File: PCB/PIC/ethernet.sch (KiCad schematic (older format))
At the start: 49 parts, among them J5 RJ45-TRANSFO, U1 LAN_8740, U2 SI502

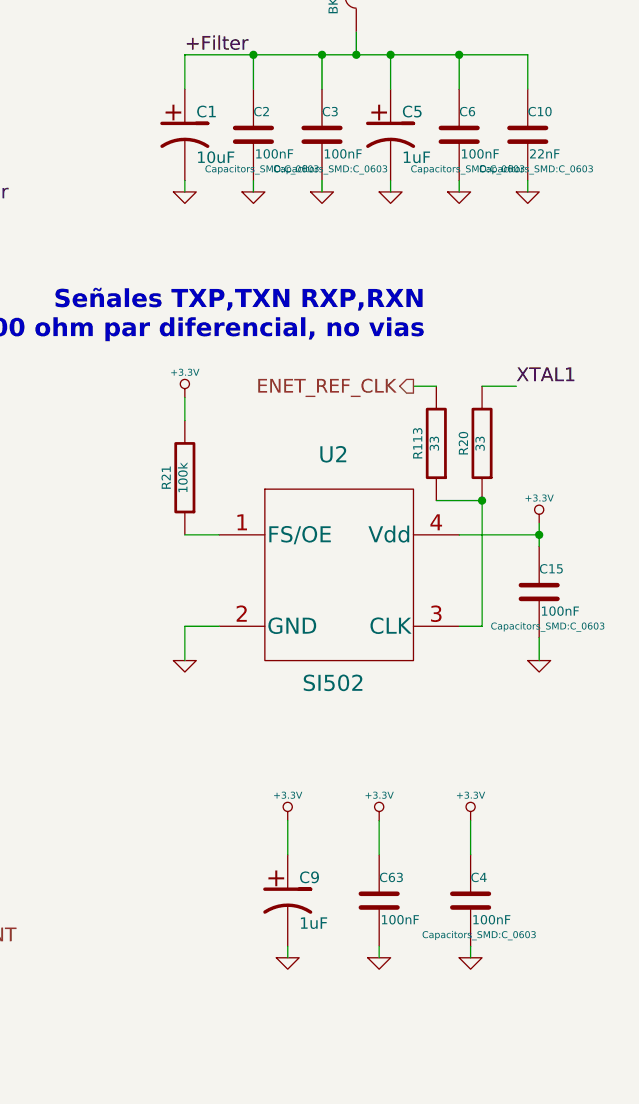
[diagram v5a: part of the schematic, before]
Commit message: rev02 se completa campo num. de frabicante(manf#) CIAA-PIC
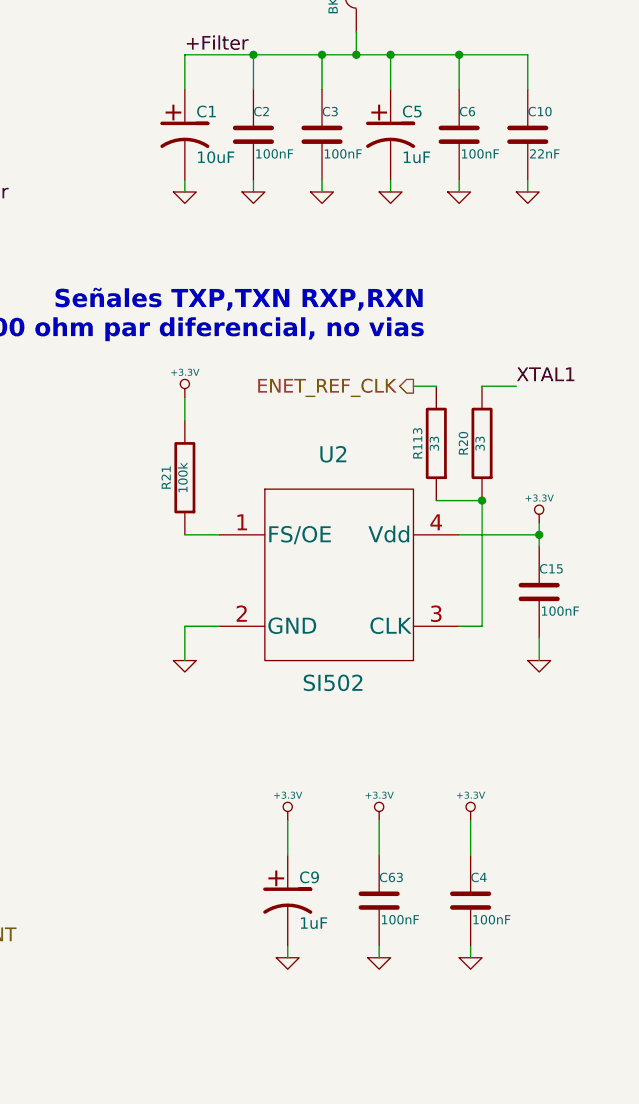
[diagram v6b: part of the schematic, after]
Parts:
- C15, C2, C3, C4, C6, C63: manf# (none) -> C0603C104K5RACTU
- L1: footprint (none) -> footprints:SM0603; manf# (none) -> MH1608-221Y
- R1: manf# (none) -> 311-1.5KGRCT-ND
- R10, R11, R12: manf# (none) -> RC0603JR-0722RL
- R113, R140, R20: manf# (none) -> RC0603JR-0733RL
- R13, R14, R7, R8, R9: manf# (none) -> RC0603JR-070RL
- R139, R2, R31, R81, R91, R95: manf# (none) -> RC0603FR-074K7L
- R15, R16, R92: manf# (none) -> RC0603JR-0710KL
- R17, R18: manf# (none) -> RC0603JR-07270RL
- R19: manf# (none) -> RC0603FR-0712K1L
- R21: manf# (none) -> RC0603JR-07100KL
- R3, R4, R5, R6: #manf RC0603FR-0749R9L -> (none); manf# (none) -> RC0603FR-0749R9L
- U1: manf# (none) -> LAN8740A-EN
- U2: manf# (none) -> 502AAA-ADAG
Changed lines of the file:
@@
 F 0 "C6" H 10350 2350 40  0000 L CNN
 F 1 "100nF" H 10356 2165 40  0000 L CNN
-F 2 "Capacitors_SMD:C_0603" H 10388 2100 30  0000 C CNN
+F 2 "Capacitors_SMD:C_0603" H 10388 2100 30  0001 C CNN
 F 3 "~" H 10350 2250 60  0000 C CNN
+F 4 "C0603C104K5RACTU " H 10350 2250 60  0001 C CNN "manf#"
 	1    10350 2250
 	1    0    0    -1
@@
 F 0 "C2" H 9450 2350 40  0000 L CNN
 F 1 "100nF" H 9456 2165 40  0000 L CNN
-F 2 "Capacitors_SMD:C_0603" H 9488 2100 30  0000 C CNN
+F 2 "Capacitors_SMD:C_0603" H 9488 2100 30  0001 C CNN
 F 3 "~" H 9450 2250 60  0000 C CNN
+F 4 "C0603C104K5RACTU " H 9450 2250 60  0001 C CNN "manf#"
 	1    9450 2250
 	1    0    0    -1
@@
 F 0 "C3" H 9750 2350 40  0000 L CNN
 F 1 "100nF" H 9756 2165 40  0000 L CNN
-F 2 "Capacitors_SMD:C_0603" H 9788 2100 30  0000 C CNN
+F 2 "Capacitors_SMD:C_0603" H 9788 2100 30  0001 C CNN
 F 3 "~" H 9750 2250 60  0000 C CNN
+F 4 "C0603C104K5RACTU " H 9750 2250 60  0001 C CNN "manf#"
 	1    9750 2250
 	1    0    0    -1
@@
 F 2 "Resistors_SMD:R_0603" V 2480 4200 30  0001 C CNN
 F 3 "~" H 2550 4200 30  0000 C CNN
+F 4 "RC0603FR-074K7L" V 2550 4200 60  0001 C CNN "manf#"
 	1    2550 4200
 	1    0    0    -1
@@
 F 2 "Resistors_SMD:R_0603" V 2730 1650 30  0001 C CNN
 F 3 "~" H 2800 1650 30  0000 C CNN
+F 4 "311-1.5KGRCT-ND" V 2800 1650 60  0001 C CNN "manf#"
 	1    2800 1650
 	1    0    0    -1
@@
 F 2 "Resistors_SMD:R_0603" V 6980 2850 30  0001 C CNN
 F 3 "~" H 7050 2850 30  0000 C CNN
-F 4 "RC0603FR-0749R9L" V 7050 2850 60  0001 C CNN "#manf"
+F 4 "RC0603FR-0749R9L" V 7050 2850 60  0001 C CNN "manf#"
 	1    7050 2850
 	1    0    0    -1
@@
 F 2 "Resistors_SMD:R_0603" V 7230 2850 30  0001 C CNN
 F 3 "~" H 7300 2850 30  0000 C CNN
-F 4 "RC0603FR-0749R9L" V 7300 2850 60  0001 C CNN "#manf"
+F 4 "RC0603FR-0749R9L" V 7300 2850 60  0001 C CNN "manf#"
 	1    7300 2850
 	1    0    0    -1
@@
 F 2 "Resistors_SMD:R_0603" V 7580 2850 30  0001 C CNN
 F 3 "~" H 7650 2850 30  0000 C CNN
-F 4 "RC0603FR-0749R9L" V 7650 2850 60  0001 C CNN "#manf"
+F 4 "RC0603FR-0749R9L" V 7650 2850 60  0001 C CNN "manf#"
 	1    7650 2850
 	1    0    0    -1
@@
 F 2 "Resistors_SMD:R_0603" V 7780 2850 30  0001 C CNN
 F 3 "~" H 7850 2850 30  0000 C CNN
-F 4 "RC0603FR-0749R9L" V 7850 2850 60  0001 C CNN "#manf"
+F 4 "RC0603FR-0749R9L" V 7850 2850 60  0001 C CNN "manf#"
 	1    7850 2850
 	1    0    0    -1
@@
 F 0 "C10" H 10650 2350 40  0000 L CNN
 F 1 "22nF" H 10656 2165 40  0000 L CNN
-F 2 "Capacitors_SMD:C_0603" H 10688 2100 30  0000 C CNN
+F 2 "Capacitors_SMD:C_0603" H 10688 2100 30  0001 C CNN
 F 3 "~" H 10650 2250 60  0000 C CNN
 	1    10650 2250
@@
 F 2 "Resistors_SMD:R_0603" V 780 6800 30  0001 C CNN
 F 3 "~" H 850 6800 30  0000 C CNN
+F 4 "RC0603JR-07270RL" V 850 6800 60  0001 C CNN "manf#"
 	1    850  6800
 	-1   0    0    1
@@
 F 2 "Resistors_SMD:R_0603" V 980 6800 30  0001 C CNN
 F 3 "~" H 1050 6800 30  0000 C CNN
+F 4 "RC0603JR-07270RL" V 1050 6800 60  0001 C CNN "manf#"
 	1    1050 6800
 	-1   0    0    1
@@
 F 2 "Resistors_SMD:R_0603" V 7230 5650 30  0001 C CNN
 F 3 "~" H 7300 5650 30  0000 C CNN
+F 4 "RC0603FR-0712K1L " V 7300 5650 60  0001 C CNN "manf#"
 	1    7300 5650
 	1    0    0    -1
@@
 F 0 "C15" H 10700 4350 40  0000 L CNN
 F 1 "100nF" H 10706 4165 40  0000 L CNN
-F 2 "Capacitors_SMD:C_0603" H 10738 4100 30  0000 C CNN
+F 2 "Capacitors_SMD:C_0603" H 10738 4100 30  0001 C CNN
 F 3 "~" H 10700 4250 60  0000 C CNN
+F 4 "C0603C104K5RACTU" H 10700 4250 60  0001 C CNN "manf#"
 	1    10700 4250
 	1    0    0    -1
@@
 F 2 "Resistors_SMD:R_0603" V 1780 2900 30  0001 C CNN
 F 3 "~" H 1850 2900 30  0000 C CNN
+F 4 "RC0603JR-070RL" V 1850 2900 60  0001 C CNN "manf#"
 	1    1850 2900
 	0    -1   -1   0
@@
 F 2 "Resistors_SMD:R_0603" V 1780 3000 30  0001 C CNN
 F 3 "~" H 1850 3000 30  0000 C CNN
+F 4 "RC0603JR-070RL" V 1850 3000 60  0001 C CNN "manf#"
 	1    1850 3000
 	0    -1   -1   0
@@
 F 2 "Resistors_SMD:R_0603" V 1780 2800 30  0001 C CNN
 F 3 "~" H 1850 2800 30  0000 C CNN
+F 4 "RC0603JR-070RL" V 1850 2800 60  0001 C CNN "manf#"
 	1    1850 2800
 	0    -1   -1   0
@@
 F 2 "Resistors_SMD:R_0603" V 1780 2700 30  0001 C CNN
 F 3 "~" H 1850 2700 30  0000 C CNN
+F 4 "RC0603JR-0722RL" V 1850 2700 60  0001 C CNN "manf#"
 	1    1850 2700
 	0    -1   -1   0
@@
 F 2 "Resistors_SMD:R_0603" V 1780 2600 30  0001 C CNN
 F 3 "~" H 1850 2600 30  0000 C CNN
+F 4 "RC0603JR-0722RL" V 1850 2600 60  0001 C CNN "manf#"
 	1    1850 2600
 	0    -1   -1   0
@@
 F 2 "Resistors_SMD:R_0603" V 1930 4550 30  0001 C CNN
 F 3 "~" H 2000 4550 30  0000 C CNN
+F 4 "RC0603JR-0722RL" V 2000 4550 60  0001 C CNN "manf#"
 	1    2000 4550
 	0    -1   -1   0
@@
 F 2 "Resistors_SMD:R_0603" V 1780 2200 30  0001 C CNN
 F 3 "~" H 1850 2200 30  0000 C CNN
+F 4 " RC0603JR-070RL" V 1850 2200 60  0001 C CNN "manf#"
 	1    1850 2200
 	0    -1   -1   0
@@
 F 2 "Resistors_SMD:R_0603" V 1780 2300 30  0001 C CNN
 F 3 "~" H 1850 2300 30  0000 C CNN
+F 4 "RC0603JR-070RL" V 1850 2300 60  0001 C CNN "manf#"
 	1    1850 2300
 	0    -1   -1   0
@@
 F 0 "C4" H 10400 5700 40  0000 L CNN
 F 1 "100nF" H 10406 5515 40  0000 L CNN
-F 2 "Capacitors_SMD:C_0603" H 10438 5450 30  0000 C CNN
+F 2 "Capacitors_SMD:C_0603" H 10438 5450 30  0001 C CNN
 F 3 "~" H 10400 5600 60  0000 C CNN
+F 4 "C0603C104K5RACTU" H 10400 5600 60  0001 C CNN "manf#"
 	1    10400 5600
 	1    0    0    -1
@@
 F 2 "footprints:4SMD" H 9850 3650 60  0001 C CNN
 F 3 "http://www.digikey.com/product-detail/en/silicon-labs/502AAA-ADAG/502AAA-ADAG-ND/4173092" H 8750 7500 60  0001 C CNN
+F 4 "502AAA-ADAG" H 9800 4200 60  0001 C CNN "manf#"
 	1    9800 4200
 	1    0    0    -1
@@
 F 2 "Resistors_SMD:R_0603" V 10380 3600 30  0001 C CNN
 F 3 "~" H 10450 3600 30  0000 C CNN
+F 4 "RC0603JR-0733RL" V 10450 3600 60  0001 C CNN "manf#"
 	1    10450 3600
 	-1   0    0    1
@@
 F 2 "Resistors_SMD:R_0603" V 1780 2500 30  0001 C CNN
 F 3 "~" H 1850 2500 30  0000 C CNN
+F 4 " RC0603JR-0710KL" V 1850 2500 60  0001 C CNN "manf#"
 	1    1850 2500
 	0    -1   -1   0
@@
 F 2 "Resistors_SMD:R_0603" V 7830 5400 30  0001 C CNN
 F 3 "~" H 7900 5400 30  0000 C CNN
+F 4 " RC0603JR-0710KL" V 7900 5400 60  0001 C CNN "manf#"
 	1    7900 5400
 	1    0    0    -1
@@
 F 2 "Resistors_SMD:R_0603" V 9080 3750 30  0001 C CNN
 F 3 "~" H 9150 3750 30  0000 C CNN
+F 4 "RC0603JR-07100KL" V 9150 3750 60  0001 C CNN "manf#"
 	1    9150 3750
 	-1   0    0    1
@@
 F 2 "Resistors_SMD:R_0603" V 2330 1650 30  0001 C CNN
 F 3 "~" H 2400 1650 30  0000 C CNN
+F 4 "RC0603FR-074K7L " V 2400 1650 60  0001 C CNN "manf#"
 	1    2400 1650
 	1    0    0    -1
@@
 F 2 "Capacitors_SMD:C_0603" H 10038 5450 30  0001 C CNN
 F 3 "~" H 10000 5600 60  0000 C CNN
+F 4 "C0603C104K5RACTU" H 10000 5600 60  0001 C CNN "manf#"
 	1    10000 5600
 	1    0    0    -1
@@
 F 2 "Resistors_SMD:R_0603" V 2130 1650 30  0001 C CNN
 F 3 "~" H 2200 1650 30  0000 C CNN
+F 4 "RC0603FR-074K7L " V 2200 1650 60  0001 C CNN "manf#"
 	1    2200 1650
 	1    0    0    -1
@@
 F 2 "Resistors_SMD:R_0603" V 1780 3300 30  0001 C CNN
 F 3 "~" H 1850 3300 30  0000 C CNN
+F 4 "RC0603FR-074K7L " V 1850 3300 60  0001 C CNN "manf#"
 	1    1850 3300
 	0    -1   -1   0
@@
 F 2 "Resistors_SMD:R_0603" V 1780 3200 30  0001 C CNN
 F 3 "~" H 1850 3200 30  0000 C CNN
+F 4 "RC0603FR-074K7L " V 1850 3200 60  0001 C CNN "manf#"
 	1    1850 3200
 	0    -1   -1   0
@@
 F 2 "Resistors_SMD:R_0603" V 1780 2400 30  0001 C CNN
 F 3 "~" H 1850 2400 30  0000 C CNN
+F 4 "RC0603FR-074K7L " V 1850 2400 60  0001 C CNN "manf#"
 	1    1850 2400
 	0    -1   -1   0
@@
 F 2 "Resistors_SMD:R_0603" V 2580 3300 30  0001 C CNN
 F 3 "~" H 2650 3300 30  0000 C CNN
+F 4 "RC0603JR-0733RL " V 2650 3300 60  0001 C CNN "manf#"
 	1    2650 3300
 	0    -1   -1   0
@@
 F 2 "Resistors_SMD:R_0603" V 2530 1650 30  0001 C CNN
 F 3 "~" H 2600 1650 30  0000 C CNN
+F 4 " RC0603JR-0710KL" V 2600 1650 60  0001 C CNN "manf#"
 	1    2600 1650
 	1    0    0    -1
@@
 F 2 "Resistors_SMD:R_0603" V 10180 3600 30  0001 C CNN
 F 3 "~" H 10250 3600 30  0000 C CNN
+F 4 "RC0603JR-0733RL" V 10250 3600 60  0001 C CNN "manf#"
 	1    10250 3600
 	-1   0    0    1
@@
 F 2 "footprints:QFN32_Opendous" H 6450 2000 60  0001 C CNN
 F 3 "http://www.digikey.hk/product-detail/en/microchip-technology/LAN8740AI-EN/LAN8740AI-EN-ND/4079781" H 6050 6150 60  0001 C CNN
+F 4 "LAN8740A-EN" H 5750 3850 60  0001 C CNN "manf#"
 	1    5750 3850
 	1    0    0    -1
@@
 F 0 "L1" V 9850 1500 40  0000 C CNN
 F 1 "BK1608HS220-T" V 10000 1500 40  0000 C CNN
-F 2 "" H 9900 1500 60  0001 C CNN
+F 2 "footprints:SM0603" H 9900 1500 60  0001 C CNN
 F 3 "~" H 9900 1500 60  0000 C CNN
+F 4 "MH1608-221Y" V 9900 1500 60  0001 C CNN "manf#"
 	1    9900 1500
 	-1   0    0    1

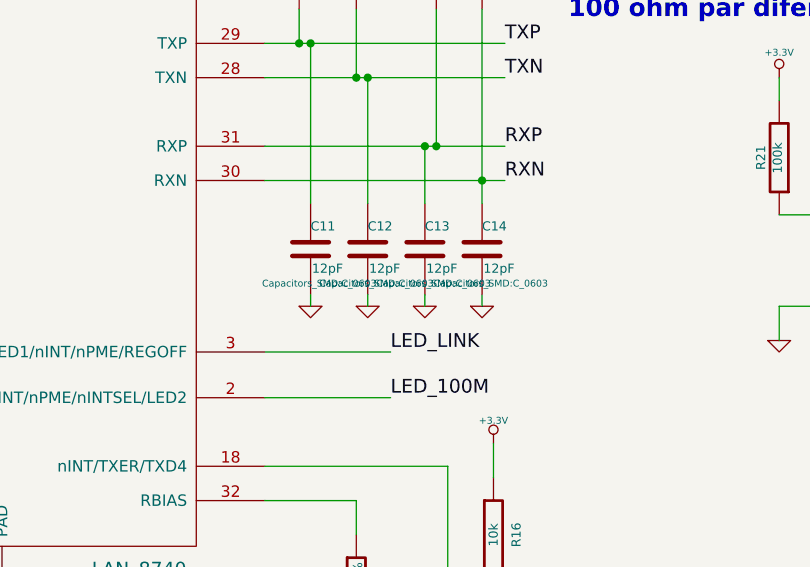
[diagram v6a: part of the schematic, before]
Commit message: se completa campo num. de frabicante(manf#) CIAA-PIC
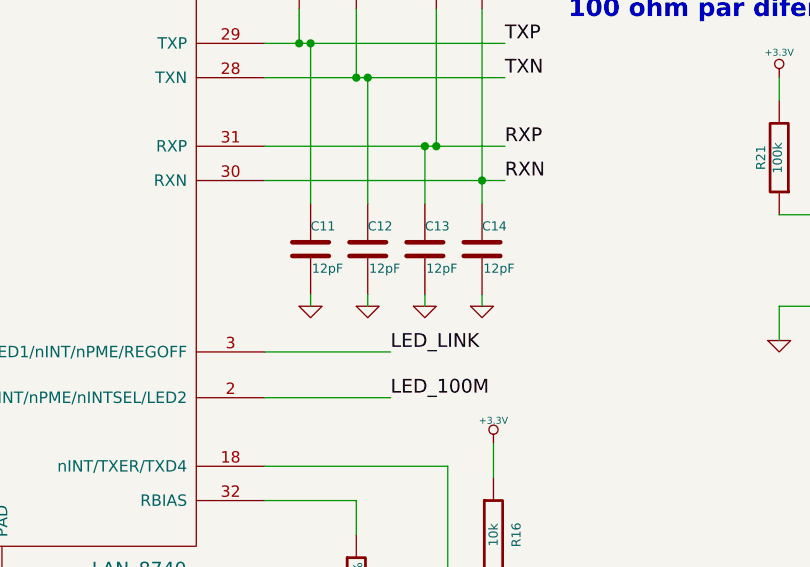
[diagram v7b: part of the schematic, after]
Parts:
- C1: footprint (none) -> footprints:c_1206_tantalio; manf# (none) -> T491A106K006AT
- C11, C12, C13, C14: manf# (none) -> CBR02C120F3GAC
- C5, C8, C9: footprint (none) -> footprints:c_0603; manf# (none) -> C0603C105K9PACTU
- C7: manf# (none) -> C0603C471K5RACTU
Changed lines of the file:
@@
 F 2 "Capacitors_SMD:C_0603" H 6838 2000 30  0001 C CNN
 F 3 "~" H 6800 2150 60  0000 C CNN
+F 4 "C0603C471K5RACTU" H 6800 2150 60  0001 C CNN "manf#"
 	1    6800 2150
 	1    0    0    -1
@@
 F 0 "C8" H 7100 2250 40  0000 L CNN
 F 1 "1uF" H 7106 2065 40  0000 L CNN
-F 2 "" H 7138 2000 30  0001 C CNN
+F 2 "footprints:c_0603" H 7138 2000 30  0001 C CNN
 F 3 "~" H 7100 2150 60  0000 C CNN
+F 4 "C0603C105K9PACTU" H 7100 2150 60  0001 C CNN "manf#"
 	1    7100 2150
 	1    0    0    -1
@@
 F 0 "C11" H 7100 4250 40  0000 L CNN
 F 1 "12pF" H 7106 4065 40  0000 L CNN
-F 2 "Capacitors_SMD:C_0603" H 7138 4000 30  0000 C CNN
+F 2 "Capacitors_SMD:C_0603" H 7138 4000 30  0001 C CNN
 F 3 "~" H 7100 4150 60  0000 C CNN
+F 4 "CBR02C120F3GAC " H 7100 4150 60  0001 C CNN "manf#"
 	1    7100 4150
 	1    0    0    -1
@@
 F 0 "C12" H 7350 4250 40  0000 L CNN
 F 1 "12pF" H 7356 4065 40  0000 L CNN
-F 2 "Capacitors_SMD:C_0603" H 7388 4000 30  0000 C CNN
+F 2 "Capacitors_SMD:C_0603" H 7388 4000 30  0001 C CNN
 F 3 "~" H 7350 4150 60  0000 C CNN
+F 4 "CBR02C120F3GAC " H 7350 4150 60  0001 C CNN "manf#"
 	1    7350 4150
 	1    0    0    -1
@@
 F 0 "C13" H 7600 4250 40  0000 L CNN
 F 1 "12pF" H 7606 4065 40  0000 L CNN
-F 2 "Capacitors_SMD:C_0603" H 7638 4000 30  0000 C CNN
+F 2 "Capacitors_SMD:C_0603" H 7638 4000 30  0001 C CNN
 F 3 "~" H 7600 4150 60  0000 C CNN
+F 4 "CBR02C120F3GAC " H 7600 4150 60  0001 C CNN "manf#"
 	1    7600 4150
 	1    0    0    -1
@@
 F 0 "C14" H 7850 4250 40  0000 L CNN
 F 1 "12pF" H 7856 4065 40  0000 L CNN
-F 2 "Capacitors_SMD:C_0603" H 7888 4000 30  0000 C CNN
+F 2 "Capacitors_SMD:C_0603" H 7888 4000 30  0001 C CNN
 F 3 "~" H 7850 4150 60  0000 C CNN
+F 4 "CBR02C120F3GAC " H 7850 4150 60  0001 C CNN "manf#"
 	1    7850 4150
 	1    0    0    -1
@@
 F 0 "C5" H 10100 2350 50  0000 L CNN
 F 1 "1uF" H 10100 2150 50  0000 L CNN
-F 2 "" H 10050 2250 60  0001 C CNN
+F 2 "footprints:c_0603" H 10050 2250 60  0001 C CNN
 F 3 "~" H 10050 2250 60  0000 C CNN
+F 4 "C0603C105K9PACTU" H 10050 2250 60  0001 C CNN "manf#"
 	1    10050 2250
 	1    0    0    -1
@@
 F 0 "C1" H 9200 2350 50  0000 L CNN
 F 1 "10uF" H 9200 2150 50  0000 L CNN
-F 2 "" H 9150 2250 60  0001 C CNN
+F 2 "footprints:c_1206_tantalio" H 9150 2250 60  0001 C CNN
 F 3 "~" H 9150 2250 60  0000 C CNN
+F 4 "T491A106K006AT" H 9150 2250 60  0001 C CNN "manf#"
 	1    9150 2250
 	1    0    0    -1
@@
 F 0 "C9" H 9650 5700 50  0000 L CNN
 F 1 "1uF" H 9650 5500 50  0000 L CNN
-F 2 "" H 9600 5600 60  0001 C CNN
+F 2 "footprints:c_0603" H 9600 5600 60  0001 C CNN
 F 3 "~" H 9600 5600 60  0000 C CNN
+F 4 "C0603C105K9PACTU" H 9600 5600 60  0001 C CNN "manf#"
 	1    9600 5600
 	1    0    0    -1
